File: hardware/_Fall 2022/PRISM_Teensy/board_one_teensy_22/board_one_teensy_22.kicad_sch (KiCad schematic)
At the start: 15 parts, among them J1 EAST, J2 CORE_IO, J3 USB_micro, U1 Teensy4.1, U2 BNO055_Breakout, U3 3966

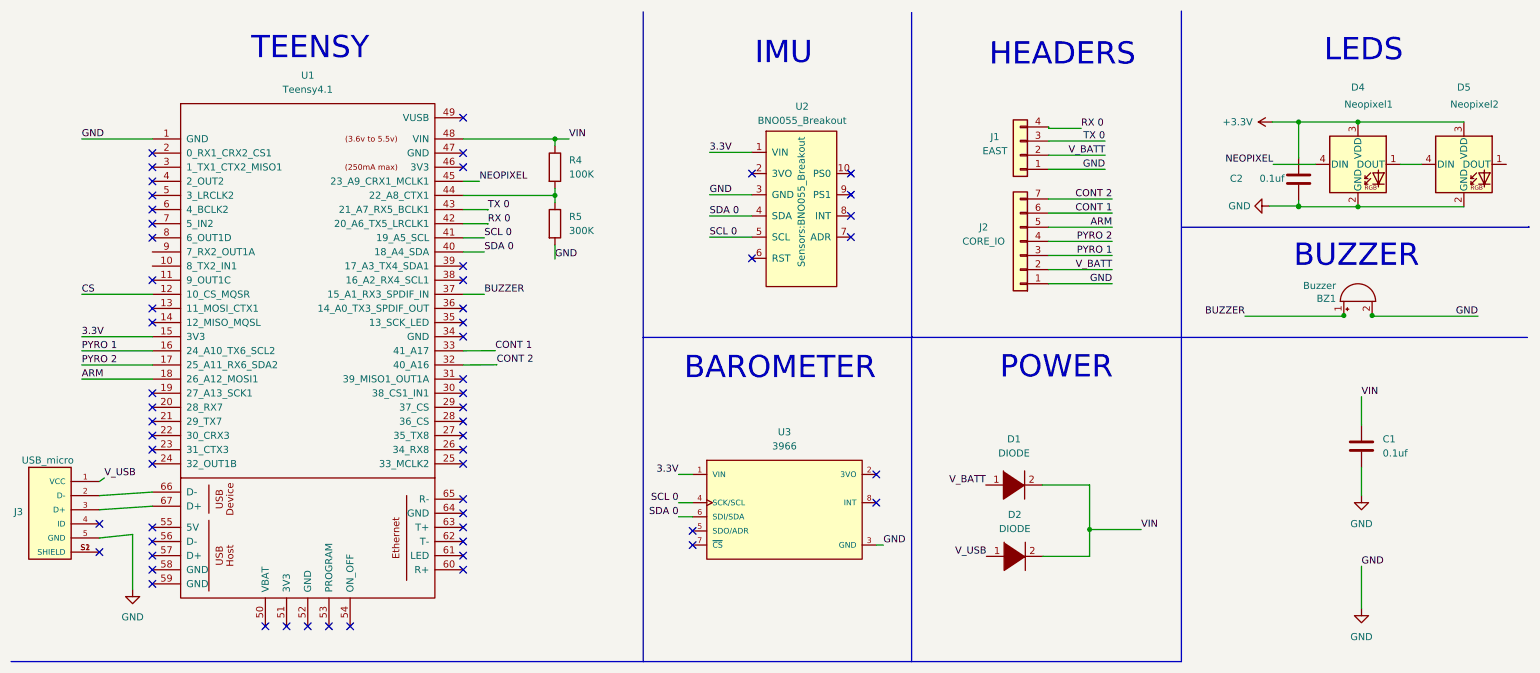
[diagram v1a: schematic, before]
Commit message: Rough layout of main teensy board
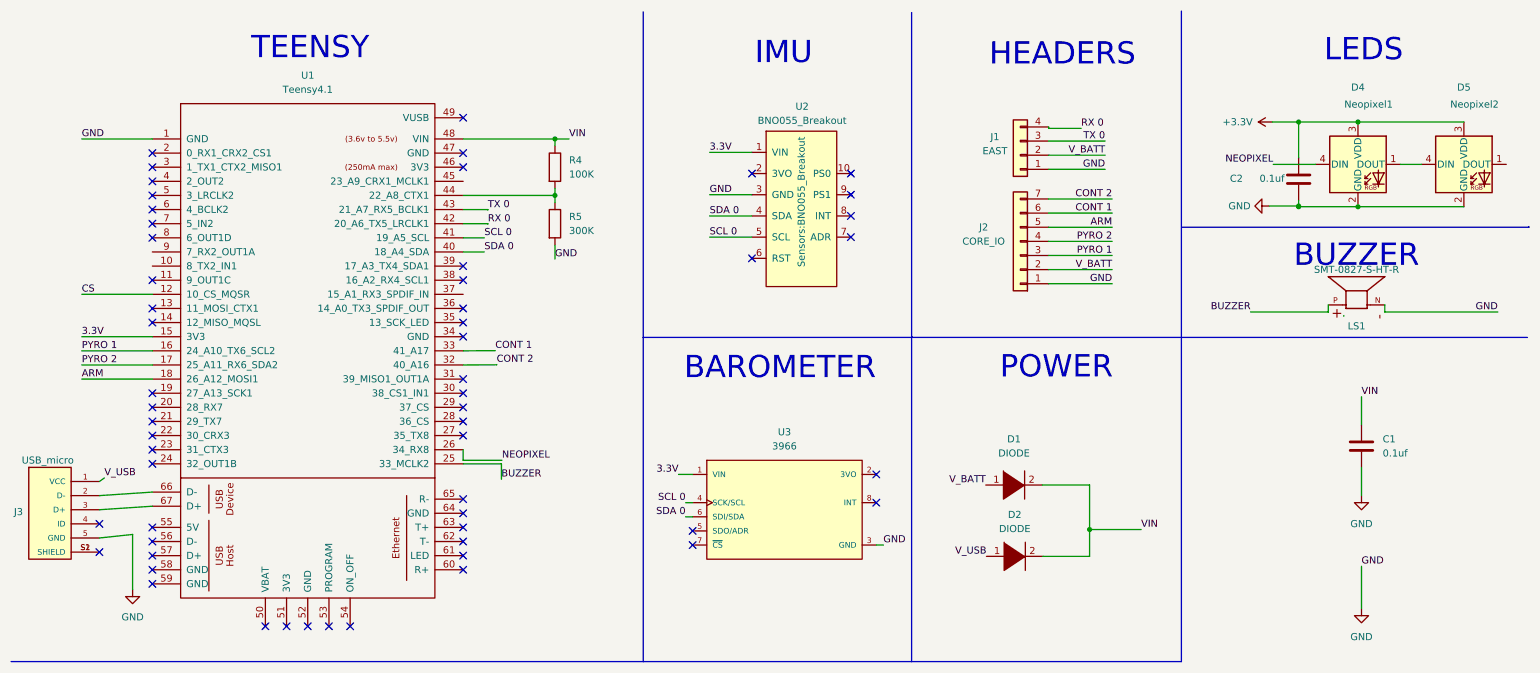
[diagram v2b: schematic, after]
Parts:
- removed BZ1: Buzzer, Olin_Rocketry:Large_Buzzer_24mmOD_14.8mmPinDistance_1.0mmPinDiameter, symbol Device:Buzzer
- added LS1: SMT-0827-S-HT-R, buzzer:XDCR_SMT-0827-S-HT-R, symbol Device:SMT-0827-S-HT-R
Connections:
- net BUZZER: now also U1.25 (33_MCLK2), LS1.P; no longer U1.37 (15_A1_RX3_SPDIF_IN)
- net GND: now also LS1.N
- net NEOPIXEL: now also U1.26 (34_RX8); no longer U1.45 (23_A9_CRX1_MCLK1)
- no-connect marks 59 -> 57
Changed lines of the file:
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@@
   (junction (at 243.586 46.99) (diameter 0) (color 0 0 0 0)
   )
-  (junction (at 256.794 66.675) (diameter 0) (color 0 0 0 0)
-  )
   (junction (at 109.855 45.085) (diameter 0) (color 0 0 0 0)
   )
   (junction (at 254.254 47.117) (diameter 0) (color 0 0 0 0)
-  )
-  (junction (at 251.714 66.675) (diameter 0) (color 0 0 0 0)
   )
   (junction (at 243.586 31.877) (diameter 0) (color 0 0 0 0)
@@
   (no_connect (at 93.345 102.235))
   (no_connect (at 93.345 99.695))
-  (no_connect (at 93.345 93.345))
-  (no_connect (at 93.345 90.805))
   (no_connect (at 93.345 88.265))
   (no_connect (at 93.345 85.725))
@@
     (stroke (width 0) (type default) (color 0 0 0 0))
   )
+  (wire (pts (xy 259.08 66.04) (xy 259.08 64.77))
+    (stroke (width 0) (type default) (color 0 0 0 0))
+  )
   (wire (pts (xy 251.714 66.675) (xy 251.714 66.802))
     (stroke (width 0) (type default) (color 0 0 0 0))
@@
     (stroke (width 0) (type default) (color 0 0 0 0))
   )
-  (wire (pts (xy 132.08 100.33) (xy 134.62 100.33))
+  (wire (pts (xy 133.35 100.33) (xy 134.62 100.33))
     (stroke (width 0) (type default) (color 0 0 0 0))
   )
@@
     (stroke (width 0) (type default) (color 0 0 0 0))
   )
+  (wire (pts (xy 100.33 92.71) (xy 93.345 92.71))
+    (stroke (width 0) (type default) (color 0 0 0 0))
+  )
   (wire (pts (xy 97.7931 47.625) (xy 97.7931 47.6946))
     (stroke (width 0) (type default) (color 0 0 0 0))
@@
     (stroke (width 0) (type default) (color 0 0 0 0))
   )
-  (wire (pts (xy 93.345 42.545) (xy 96.2803 42.545))
-    (stroke (width 0) (type default) (color 0 0 0 0))
-  )
   (polyline (pts (xy 173.99 128.905) (xy 173.99 70.358))
     (stroke (width 0) (type default) (color 0 0 0 0))
@@
     (stroke (width 0) (type default) (color 0 0 0 0))
   )
+  (wire (pts (xy 93.345 93.345) (xy 100.2343 93.345))
+    (stroke (width 0) (type default) (color 0 0 0 0))
+  )
   (wire (pts (xy 145.288 37.338) (xy 137.668 37.338))
     (stroke (width 0) (type default) (color 0 0 0 0))
@@
     (stroke (width 0) (type default) (color 0 0 0 0))
   )
-  (wire (pts (xy 132.08 102.87) (xy 134.62 102.87))
+  (wire (pts (xy 133.35 102.87) (xy 134.62 102.87))
     (stroke (width 0) (type default) (color 0 0 0 0))
   )
@@
     (stroke (width 0) (type default) (color 0 0 0 0))
   )
+  (wire (pts (xy 248.92 66.04) (xy 248.92 64.77))
+    (stroke (width 0) (type default) (color 0 0 0 0))
+  )
   (wire (pts (xy 205.994 97.155) (xy 205.994 105.156))
     (stroke (width 0) (type default) (color 0 0 0 0))
@@
     (stroke (width 0) (type default) (color 0 0 0 0))
   )
-  (wire (pts (xy 256.794 66.675) (xy 256.794 66.802))
+  (wire (pts (xy 93.345 92.71) (xy 93.345 90.805))
     (stroke (width 0) (type default) (color 0 0 0 0))
   )
@@
     (stroke (width 0) (type default) (color 0 0 0 0))
   )
-  (wire (pts (xy 251.714 66.802) (xy 233.934 66.802))
-    (stroke (width 0) (type default) (color 0 0 0 0))
-  )
-  (wire (pts (xy 93.345 62.865) (xy 97.155 62.865))
-    (stroke (width 0) (type default) (color 0 0 0 0))
-  )
-  (wire (pts (xy 256.794 66.802) (xy 275.844 66.802))
+  (wire (pts (xy 100.2343 93.345) (xy 100.2343 96.115))
+    (stroke (width 0) (type default) (color 0 0 0 0))
+  )
+  (wire (pts (xy 279.4 66.04) (xy 259.08 66.04))
     (stroke (width 0) (type default) (color 0 0 0 0))
   )
@@
   )
   (polyline (pts (xy 125.73 128.905) (xy 173.99 128.905))
+    (stroke (width 0) (type default) (color 0 0 0 0))
+  )
+  (wire (pts (xy 234.95 66.04) (xy 248.92 66.04))
     (stroke (width 0) (type default) (color 0 0 0 0))
   )
@@
     (effects (font (size 1.27 1.27)) (justify right bottom))
   )
-  (label "BUZZER" (at 233.934 66.802 180)
+  (label "BUZZER" (at 234.95 66.04 180)
     (effects (font (size 1.27 1.27)) (justify right bottom))
   )
@@
     (effects (font (size 1.27 1.27)) (justify right bottom))
   )
-  (label "BUZZER" (at 97.155 62.865 0)
-    (effects (font (size 1.27 1.27)) (justify left bottom))
-  )
-  (label "SCL 0" (at 132.08 100.33 180)
+  (label "SCL 0" (at 133.35 100.33 180)
     (effects (font (size 1.27 1.27)) (justify right bottom))
   )
@@
     (effects (font (size 1.27 1.27)) (justify right bottom))
   )
+  (label "NEOPIXEL" (at 100.33 92.71 0)
+    (effects (font (size 1.27 1.27)) (justify left bottom))
+  )
   (label "GND" (at 137.668 44.958 0)
     (effects (font (size 1.27 1.27)) (justify left bottom))
@@
     (effects (font (size 1.27 1.27)) (justify left bottom))
   )
-  (label "SDA 0" (at 132.08 102.87 180)
+  (label "SDA 0" (at 133.35 102.87 180)
     (effects (font (size 1.27 1.27)) (justify right bottom))
   )
@@
     (effects (font (size 1.27 1.27)) (justify left bottom))
   )
-  (label "GND" (at 275.844 66.802 180)
+  (label "GND" (at 279.4 66.04 180)
     (effects (font (size 1.27 1.27)) (justify right bottom))
   )
@@
     (effects (font (size 1.27 1.27)) (justify left bottom))
   )
-  (label "NEOPIXEL" (at 96.2803 42.545 0)
-    (effects (font (size 1.27 1.27)) (justify left bottom))
-  )
   (label "V_BATT" (at 187.325 97.155 180)
     (effects (font (size 1.27 1.27)) (justify right bottom))
@@
   (label "ARM" (at 210.058 50.8 180)
     (effects (font (size 1.27 1.27)) (justify right bottom))
+  )
+  (label "BUZZER" (at 100.2343 96.115 0)
+    (effects (font (size 1.27 1.27)) (justify left bottom))
   )
   (label "SCL 0" (at 137.668 52.578 0)
@@
     (pin "1")
   )
+  (symbol (lib_id "Device:SMT-0827-S-HT-R") (at 254 62.23 90) (unit 1)
+    (in_bom yes) (on_board yes)
+    (property "Reference" "LS1" (id 0) (at 254 68.58 90))
+    (property "Value" "SMT-0827-S-HT-R" (id 1) (at 254 58.42 90))
+    (property "Footprint" "buzzer:XDCR_SMT-0827-S-HT-R" (id 2) (at 242.57 62.23 0)
+      (effects (font (size 1.27 1.27)) (justify bottom) hide)
+    )
+    (property "Datasheet" "" (id 3) (at 254 62.23 0)
+      (effects (font (size 1.27 1.27)) hide)
+    )
+    (property "STANDARD" "Manufacturer Recommendations" (id 4) (at 243.84 62.23 0)
+      (effects (font (size 1.27 1.27)) (justify bottom) hide)
+    )
+    (property "MAXIMUM_PACKAGE_HEIGHT" "3.3mm" (id 5) (at 237.49 63.5 0)
+      (effects (font (size 1.27 1.27)) (justify bottom) hide)
+    )
+    (property "MANUFACTURER" "PUI Audio" (id 6) (at 238.76 63.5 0)
+      (effects (font (size 1.27 1.27)) (justify bottom) hide)
+    )
+    (property "PARTREV" "31/03/20" (id 7) (at 240.03 63.5 0)
+      (effects (font (size 1.27 1.27)) (justify bottom) hide)
+    )
+    (pin "N")
+    (pin "P")
+  )
   (symbol (lib_id "Device:C") (at 243.586 42.164 180) (unit 1)
     (in_bom yes) (on_board yes)
@@
     )
     (property "Datasheet" "~" (id 3) (at 254.889 90.17 0)
-      (effects (font (size 1.27 1.27)) hide)
-    )
-    (pin "1")
-    (pin "2")
-  )
-  (symbol (lib_id "Device:Buzzer") (at 254.254 64.135 90) (unit 1)
-    (in_bom yes) (on_board yes)
-    (property "Reference" "BZ1" (id 0) (at 250.317 63.627 90)
-      (effects (font (size 1.27 1.27)) (justify left))
-    )
-    (property "Value" "Buzzer" (id 1) (at 250.317 61.3156 90)
-      (effects (font (size 1.27 1.27)) (justify left))
-    )
-    (property "Footprint" "Olin_Rocketry:Large_Buzzer_24mmOD_14.8mmPinDistance_1.0mmPinDiameter" (id 2) (at 251.714 64.77 90)
-      (effects (font (size 1.27 1.27)) hide)
-    )
-    (property "Datasheet" "~" (id 3) (at 251.714 64.77 90)
       (effects (font (size 1.27 1.27)) hide)
     )
@@
       (reference "#PWR0102") (unit 1) (value "+3.3V") (footprint "")
     )
-    (path "/f4636155-e2e7-44c3-b6ac-e1f36ed029b8"
-      (reference "BZ1") (unit 1) (value "Buzzer") (footprint "Olin_Rocketry:Large_Buzzer_24mmOD_14.8mmPinDistance_1.0mmPinDiameter")
-    )
     (path "/ed2d98ad-ef42-4a14-aff6-3752d42a2ad5"
       (reference "C1") (unit 1) (value "0.1uf") (footprint "Capacitor_SMD:C_0201_0603Metric")
@@
       (reference "J3") (unit 1) (value "USB_micro") (footprint "USB:GCT_USB3131-30-0230-A_REVB")
     )
+    (path "/71d51463-5ace-405c-9104-715b675c45d7"
+      (reference "LS1") (unit 1) (value "SMT-0827-S-HT-R") (footprint "buzzer:XDCR_SMT-0827-S-HT-R")
+    )
     (path "/99baa0dd-fde4-4b75-83f6-a1af8f8c4b2c"

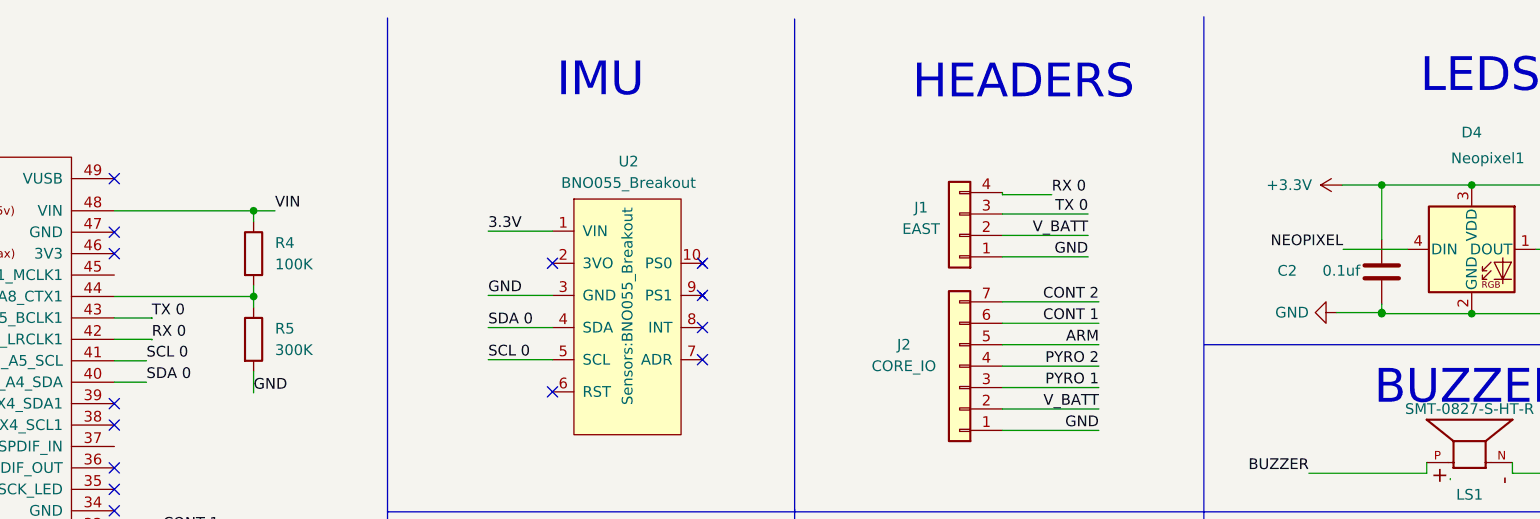
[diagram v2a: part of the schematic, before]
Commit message: Fix errors on TX/RX and added buzzer
Current state: Board 1 - need to check diodes; Board 4 - done; GPS- not showing layout traces, all need logos
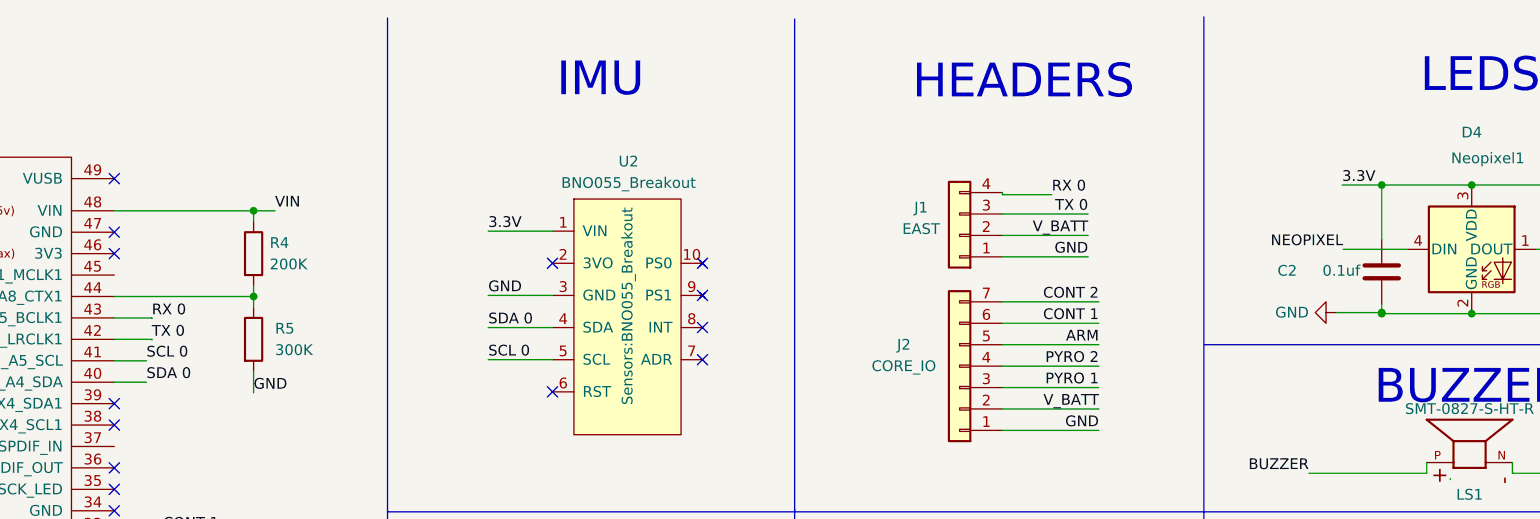
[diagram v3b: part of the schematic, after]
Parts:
- C1, C2: JLC (none) -> C307380
- R4: value 100K -> 200K; JLC (none) -> C163495
- R5: JLC (none) -> C473494
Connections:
- net +3.3V is gone; now on net 3.3V: C2.2, D4.3 (VDD), D5.3 (VDD)
- net RX 0: now also U1.43 (21_A7_RX5_BCLK1); no longer U1.42 (20_A6_TX5_LRCLK1)
- net TX 0: now also U1.42 (20_A6_TX5_LRCLK1); no longer U1.43 (21_A7_RX5_BCLK1)
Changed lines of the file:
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@@
+    (effects (font (size 1.27 1.27)) (justify left bottom))
+  )
+  (label "3.3V" (at 238.887 31.877 0)
     (effects (font (size 1.27 1.27)) (justify left bottom))
   )
@@
     (effects (font (size 1.27 1.27)) (justify right bottom))
   )
-  (label "RX 0" (at 97.7931 50.2346 0)
+  (label "TX 0" (at 97.7931 50.2346 0)
     (effects (font (size 1.27 1.27)) (justify left bottom))
   )
@@
     (effects (font (size 1.27 1.27)) (justify left bottom))
   )
-  (label "TX 0" (at 97.7931 47.6946 0)
+  (label "RX 0" (at 97.7931 47.6946 0)
     (effects (font (size 1.27 1.27)) (justify left bottom))
   )
@@
     (pin "7")
   )
-  (symbol (lib_id "power:+3.3V") (at 238.887 31.877 90) (unit 1)
-    (in_bom yes) (on_board yes) (fields_autoplaced)
-    (property "Reference" "#PWR0102" (id 0) (at 242.697 31.877 0)
-      (effects (font (size 1.27 1.27)) hide)
-    )
-    (property "Value" "+3.3V" (id 1) (at 235.331 31.8769 90)
-      (effects (font (size 1.27 1.27)) (justify left))
-    )
-    (property "Footprint" "" (id 2) (at 238.887 31.877 0)
-      (effects (font (size 1.27 1.27)) hide)
-    )
-    (property "Datasheet" "" (id 3) (at 238.887 31.877 0)
-      (effects (font (size 1.27 1.27)) hide)
-    )
-    (pin "1")
-  )
   (symbol (lib_id "Device:SMT-0827-S-HT-R") (at 254 62.23 90) (unit 1)
     (in_bom yes) (on_board yes)
@@
       (effects (font (size 1.27 1.27)) hide)
     )
+    (property "JLC" "C307380" (id 4) (at 243.586 42.164 0)
+      (effects (font (size 1.27 1.27)) hide)
+    )
     (pin "1")
     (pin "2")
@@
   (symbol (lib_id "Device:R") (at 109.855 40.005 0) (unit 1)
     (in_bom yes) (on_board yes) (fields_autoplaced)
-    (property "Reference" "R4" (id 0) (at 112.395 38.7349 0)
-      (effects (font (size 1.27 1.27)) (justify left))
-    )
-    (property "Value" "100K" (id 1) (at 112.395 41.2749 0)
+    (property "Reference" "R4" (id 0) (at 111.76 38.7349 0)
+      (effects (font (size 1.27 1.27)) (justify left))
+    )
+    (property "Value" "200K" (id 1) (at 111.76 41.2749 0)
       (effects (font (size 1.27 1.27)) (justify left))
     )
@@
     )
     (property "Datasheet" "~" (id 3) (at 109.855 40.005 0)
+      (effects (font (size 1.27 1.27)) hide)
+    )
+    (property "JLC" "C163495" (id 4) (at 109.855 40.005 0)
       (effects (font (size 1.27 1.27)) hide)
     )
@@
       (effects (font (size 1.27 1.27)) hide)
     )
+    (property "JLC" "C473494" (id 4) (at 109.855 50.165 0)
+      (effects (font (size 1.27 1.27)) hide)
+    )
     (pin "1")
     (pin "2")
@@
     )
     (property "Datasheet" "~" (id 3) (at 254.889 90.17 0)
+      (effects (font (size 1.27 1.27)) hide)
+    )
+    (property "JLC" "C307380" (id 4) (at 254.889 90.17 0)
       (effects (font (size 1.27 1.27)) hide)
     )
@@
       (reference "#PWR0101") (unit 1) (value "GND") (footprint "")
     )
-    (path "/6812e601-2160-4a60-964c-57b01c9e7fec"
-      (reference "#PWR0102") (unit 1) (value "+3.3V") (footprint "")
-    )
     (path "/ed2d98ad-ef42-4a14-aff6-3752d42a2ad5"
       (reference "C1") (unit 1) (value "0.1uf") (footprint "Capacitor_SMD:C_0201_0603Metric")
@@
     )
     (path "/99baa0dd-fde4-4b75-83f6-a1af8f8c4b2c"
-      (reference "R4") (unit 1) (value "100K") (footprint "Resistor_SMD:R_0201_0603Metric")
+      (reference "R4") (unit 1) (value "200K") (footprint "Resistor_SMD:R_0201_0603Metric")
     )
     (path "/b35b9880-c31b-4cfc-ab23-116f0c0cec40"
